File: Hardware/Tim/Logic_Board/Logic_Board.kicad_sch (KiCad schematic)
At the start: 36 parts, among them J1 SOICbite, J2 USB_C_Receptacle_USB2.0, Q1 IRLML0060TRPBF, U1 RP2040, U2 W25Q64JVZP, Y1 445I23D12M00000

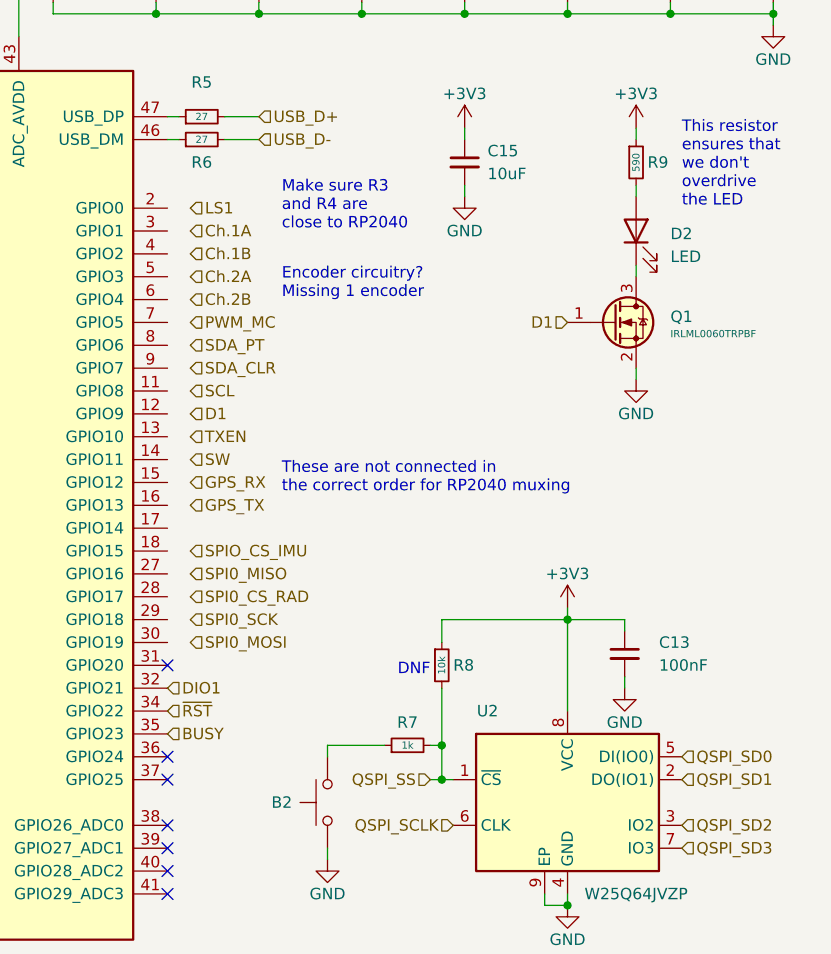
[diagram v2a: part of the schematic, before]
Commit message: Made it all one board due to large space allowed
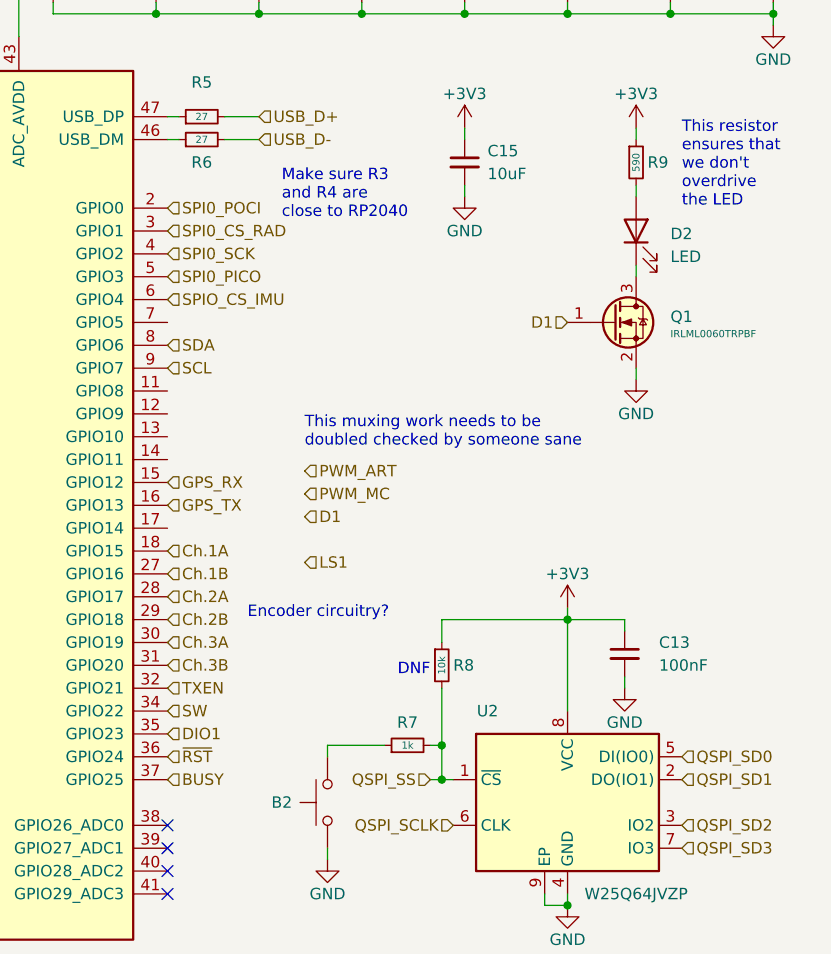
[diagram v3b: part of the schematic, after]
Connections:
- net BUSY: now also U1.37 (GPIO25); no longer U1.35 (GPIO23)
- net Ch.1A: now also U1.18 (GPIO15)
- net Ch.1B: now also U1.27 (GPIO16)
- net Ch.2A: now also U1.28 (GPIO17)
- net Ch.2B: now also U1.29 (GPIO18)
- net DIO1: now also U1.35 (GPIO23); no longer U1.32 (GPIO21)
- net GPS_RX: now also U1.15 (GPIO12)
- net GPS_TX: now also U1.16 (GPIO13)
- net SCL: now also U1.9 (GPIO7)
- net SPI0_CS_RAD: now also U1.3 (GPIO1)
- net SPI0_SCK: now also U1.4 (GPIO2)
- net SPIO_CS_IMU: now also U1.6 (GPIO4)
- net SW: now also U1.34 (GPIO22)
- net TXEN: now also U1.32 (GPIO21)
- net ~{RST}: now also U1.36 (GPIO24); no longer U1.34 (GPIO22)
- net SPI0_POCI: now reaches U1.2 (GPIO0)
- net Ch.3A: now reaches U1.30 (GPIO19)
- net Ch.3B: now reaches U1.31 (GPIO20)
- net SPI0_PICO: now reaches U1.5 (GPIO3)
- net SDA: now reaches U1.8 (GPIO6)
- no-connect marks 13 -> 10
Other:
- note added: "Encoder circuitry?"
- note added: "This muxing work needs to be doubled checked by someone sane"
- note removed: "Encoder circuitry? Missing 1 encoder"
- note removed: "These are not connected in the correct order for RP2040 muxing"
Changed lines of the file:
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@@
   (no_connect (at 20.32 132.08))
   (no_connect (at 116.84 124.46))
-  (no_connect (at 116.84 114.3))
-  (no_connect (at 116.84 101.6))
   (no_connect (at 116.84 127))
   (no_connect (at 228.6 50.8))
   (no_connect (at 20.32 127))
-  (no_connect (at 116.84 111.76))
   (wire (pts (xy 54.61 22.86) (xy 54.61 21.59))
     (stroke (width 0) (type default))
@@
     (stroke (width 0) (type default))
   )
+  (text "This muxing work needs to be \ndoubled checked by someone sane"
+    (at 132.08 77.47 0)
+    (effects (font (size 1.27 1.27)) (justify left bottom))
+  )
   (text "USB" (at 196.85 73.66 0)
     (effects (font (size 2.54 2.54) (thickness 0.508) bold) (justify left bottom))
@@
     (effects (font (size 0.8 0.8)) (justify left bottom))
   )
-  (text "Make sure R3 \nand R4 are \nclose to RP2040" (at 129.54 53.34 0)
+  (text "Make sure R3 \nand R4 are \nclose to RP2040" (at 129.54 52.07 0)
     (effects (font (size 1.27 1.27)) (justify left bottom))
   )
-  (text "Encoder circuitry?\nMissing 1 encoder" (at 129.54 60.96 0)
-    (effects (font (size 1.27 1.27)) (justify left bottom))
-  )
-  (text "These are not connected in\nthe correct order for RP2040 muxing"
-    (at 129.54 82.55 0)
+  (text "Encoder circuitry?" (at 125.73 96.52 0)
     (effects (font (size 1.27 1.27)) (justify left bottom))
   )
@@
     (effects (font (size 1.27 1.27)) (justify right bottom))
   )
-  (hierarchical_label "SW" (shape input) (at 119.38 78.74 0) (fields_autoplaced)
-    (effects (font (size 1.27 1.27)) (justify left))
-  )
-  (hierarchical_label "SDA_PT" (shape input) (at 119.38 66.04 0) (fields_autoplaced)
+  (hierarchical_label "SW" (shape input) (at 116.84 106.68 0) (fields_autoplaced)
+    (effects (font (size 1.27 1.27)) (justify left))
+  )
+  (hierarchical_label "SDA" (shape input) (at 116.84 66.04 0) (fields_autoplaced)
     (effects (font (size 1.27 1.27)) (justify left))
   )
@@
     (effects (font (size 1.27 1.27)) (justify left))
   )
-  (hierarchical_label "SPI0_SCK" (shape input) (at 119.38 96.52 0) (fields_autoplaced)
-    (effects (font (size 1.27 1.27)) (justify left))
-  )
-  (hierarchical_label "DIO1" (shape input) (at 116.84 104.14 0) (fields_autoplaced)
-    (effects (font (size 1.27 1.27)) (justify left))
-  )
-  (hierarchical_label "LS1" (shape input) (at 119.38 50.8 0) (fields_autoplaced)
+  (hierarchical_label "SPI0_SCK" (shape input) (at 116.84 55.88 0) (fields_autoplaced)
+    (effects (font (size 1.27 1.27)) (justify left))
+  )
+  (hierarchical_label "DIO1" (shape input) (at 116.84 109.22 0) (fields_autoplaced)
+    (effects (font (size 1.27 1.27)) (justify left))
+  )
+  (hierarchical_label "LS1" (shape input) (at 132.08 90.17 0) (fields_autoplaced)
     (effects (font (size 1.27 1.27)) (justify left))
   )
@@
     (effects (font (size 1.27 1.27)) (justify right))
   )
-  (hierarchical_label "BUSY" (shape input) (at 116.84 109.22 0) (fields_autoplaced)
+  (hierarchical_label "BUSY" (shape input) (at 116.84 114.3 0) (fields_autoplaced)
     (effects (font (size 1.27 1.27)) (justify left))
   )
@@
     (effects (font (size 1.27 1.27)) (justify right))
   )
+  (hierarchical_label "Ch.3A" (shape input) (at 116.84 99.06 0) (fields_autoplaced)
+    (effects (font (size 1.27 1.27)) (justify left))
+  )
   (hierarchical_label "QSPI_SD3" (shape input) (at 173.99 121.92 0) (fields_autoplaced)
     (effects (font (size 1.27 1.27)) (justify left))
@@
     (effects (font (size 1.27 1.27)) (justify right))
   )
-  (hierarchical_label "GPS_TX" (shape input) (at 119.38 83.82 0) (fields_autoplaced)
+  (hierarchical_label "GPS_TX" (shape input) (at 116.84 83.82 0) (fields_autoplaced)
     (effects (font (size 1.27 1.27)) (justify left))
   )
@@
     (effects (font (size 1.27 1.27)) (justify left))
   )
-  (hierarchical_label "Ch.1A" (shape input) (at 119.38 53.34 0) (fields_autoplaced)
-    (effects (font (size 1.27 1.27)) (justify left))
-  )
-  (hierarchical_label "Ch.2B" (shape input) (at 119.38 60.96 0) (fields_autoplaced)
+  (hierarchical_label "Ch.1A" (shape input) (at 116.84 88.9 0) (fields_autoplaced)
+    (effects (font (size 1.27 1.27)) (justify left))
+  )
+  (hierarchical_label "Ch.2B" (shape input) (at 116.84 96.52 0) (fields_autoplaced)
     (effects (font (size 1.27 1.27)) (justify left))
   )
@@
     (effects (font (size 1.27 1.27)) (justify left))
   )
-  (hierarchical_label "~{RST}" (shape input) (at 116.84 106.68 0) (fields_autoplaced)
-    (effects (font (size 1.27 1.27)) (justify left))
-  )
-  (hierarchical_label "D1" (shape input) (at 119.38 73.66 0) (fields_autoplaced)
-    (effects (font (size 1.27 1.27)) (justify left))
-  )
-  (hierarchical_label "SPI0_MISO" (shape input) (at 119.38 91.44 0) (fields_autoplaced)
+  (hierarchical_label "~{RST}" (shape input) (at 116.84 111.76 0) (fields_autoplaced)
+    (effects (font (size 1.27 1.27)) (justify left))
+  )
+  (hierarchical_label "D1" (shape input) (at 132.08 85.09 0) (fields_autoplaced)
+    (effects (font (size 1.27 1.27)) (justify left))
+  )
+  (hierarchical_label "SPI0_PICO" (shape input) (at 116.84 58.42 0) (fields_autoplaced)
     (effects (font (size 1.27 1.27)) (justify left))
   )
@@
     (effects (font (size 1.27 1.27)) (justify right))
   )
-  (hierarchical_label "SPI0_CS_RAD" (shape input) (at 119.38 93.98 0) (fields_autoplaced)
-    (effects (font (size 1.27 1.27)) (justify left))
-  )
-  (hierarchical_label "Ch.1B" (shape input) (at 119.38 55.88 0) (fields_autoplaced)
-    (effects (font (size 1.27 1.27)) (justify left))
-  )
-  (hierarchical_label "SCL" (shape input) (at 119.38 71.12 0) (fields_autoplaced)
-    (effects (font (size 1.27 1.27)) (justify left))
-  )
-  (hierarchical_label "SPIO_CS_IMU" (shape input) (at 119.38 88.9 0) (fields_autoplaced)
-    (effects (font (size 1.27 1.27)) (justify left))
-  )
-  (hierarchical_label "Ch.2A" (shape input) (at 119.38 58.42 0) (fields_autoplaced)
-    (effects (font (size 1.27 1.27)) (justify left))
-  )
-  (hierarchical_label "GPS_RX" (shape input) (at 119.38 81.28 0) (fields_autoplaced)
-    (effects (font (size 1.27 1.27)) (justify left))
-  )
-  (hierarchical_label "SPI0_MOSI" (shape input) (at 119.38 99.06 0) (fields_autoplaced)
+  (hierarchical_label "SPI0_CS_RAD" (shape input) (at 116.84 53.34 0) (fields_autoplaced)
+    (effects (font (size 1.27 1.27)) (justify left))
+  )
+  (hierarchical_label "Ch.1B" (shape input) (at 116.84 91.44 0) (fields_autoplaced)
+    (effects (font (size 1.27 1.27)) (justify left))
+  )
+  (hierarchical_label "SCL" (shape input) (at 116.84 68.58 0) (fields_autoplaced)
+    (effects (font (size 1.27 1.27)) (justify left))
+  )
+  (hierarchical_label "SPIO_CS_IMU" (shape input) (at 116.84 60.96 0) (fields_autoplaced)
+    (effects (font (size 1.27 1.27)) (justify left))
+  )
+  (hierarchical_label "Ch.2A" (shape input) (at 116.84 93.98 0) (fields_autoplaced)
+    (effects (font (size 1.27 1.27)) (justify left))
+  )
+  (hierarchical_label "PWM_ART" (shape input) (at 132.08 80.01 0) (fields_autoplaced)
+    (effects (font (size 1.27 1.27)) (justify left))
+  )
+  (hierarchical_label "GPS_RX" (shape input) (at 116.84 81.28 0) (fields_autoplaced)
+    (effects (font (size 1.27 1.27)) (justify left))
+  )
+  (hierarchical_label "SPI0_POCI" (shape input) (at 116.84 50.8 0) (fields_autoplaced)
     (effects (font (size 1.27 1.27)) (justify left))
   )
@@
     (effects (font (size 1.27 1.27)) (justify left))
   )
-  (hierarchical_label "TXEN" (shape input) (at 119.38 76.2 0) (fields_autoplaced)
-    (effects (font (size 1.27 1.27)) (justify left))
-  )
-  (hierarchical_label "SDA_CLR" (shape input) (at 119.38 68.58 0) (fields_autoplaced)
+  (hierarchical_label "TXEN" (shape input) (at 116.84 104.14 0) (fields_autoplaced)
     (effects (font (size 1.27 1.27)) (justify left))
   )
@@
     (effects (font (size 1.27 1.27)) (justify left))
   )
+  (hierarchical_label "Ch.3B" (shape input) (at 116.84 101.6 0) (fields_autoplaced)
+    (effects (font (size 1.27 1.27)) (justify left))
+  )
   (hierarchical_label "USB_D-" (shape input) (at 256.54 43.18 0) (fields_autoplaced)
     (effects (font (size 1.27 1.27)) (justify left))
   )
-  (hierarchical_label "PWM_MC" (shape input) (at 119.38 63.5 0) (fields_autoplaced)
-    (effects (font (size 1.27 1.27)) (justify left))
-  )
+  (hierarchical_label "PWM_MC" (shape input) (at 132.08 82.55 0) (fields_autoplaced)
+    (effects (font (size 1.27 1.27)) (justify left))
+  )
